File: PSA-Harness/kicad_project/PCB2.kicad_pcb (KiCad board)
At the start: 4 copper layers, 28.3 x 54 mm, 15 parts, among them J1 to_EPS_1, J2 to_EPS_2, J3 to_ESP_3, J7 USB_C_Receptacle, J8 B2B_1, J9 B2B_2, U1 DG419LEUA, U2 DG419LEUA

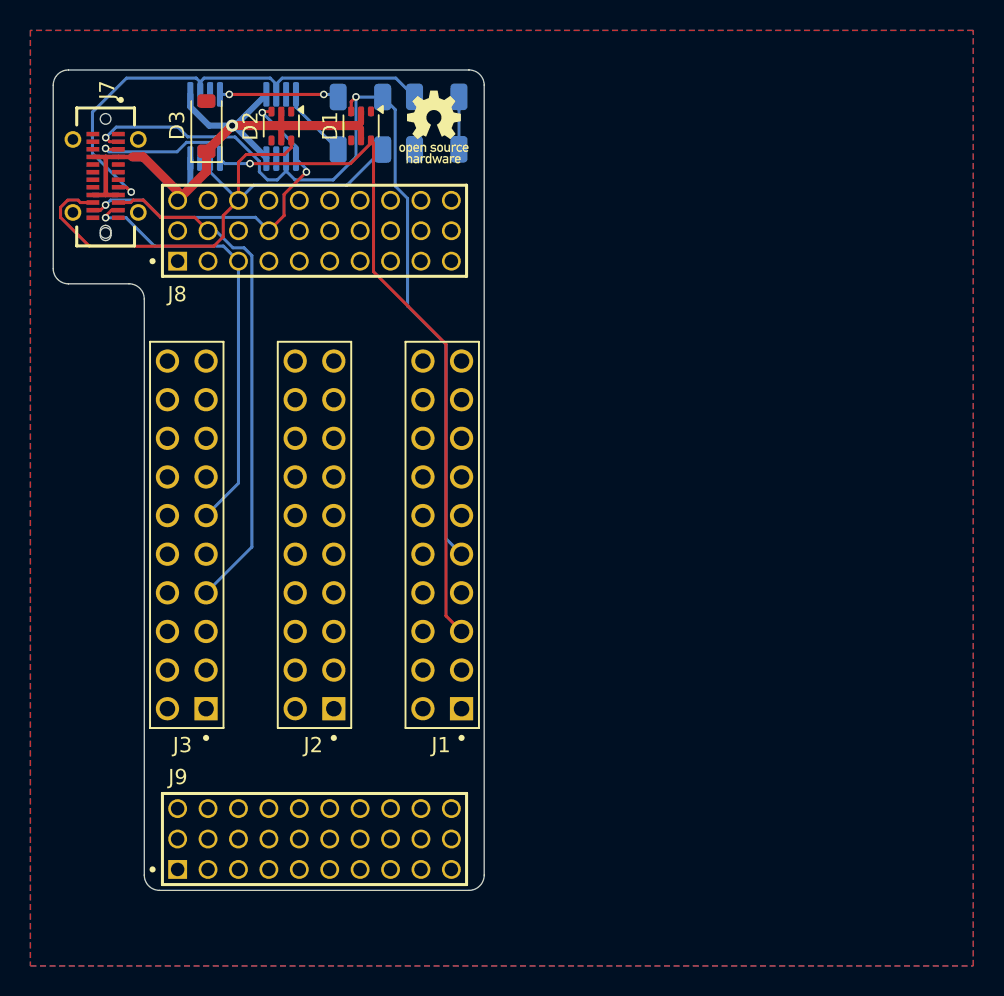
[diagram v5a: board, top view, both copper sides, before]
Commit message: PCB1/2 routed
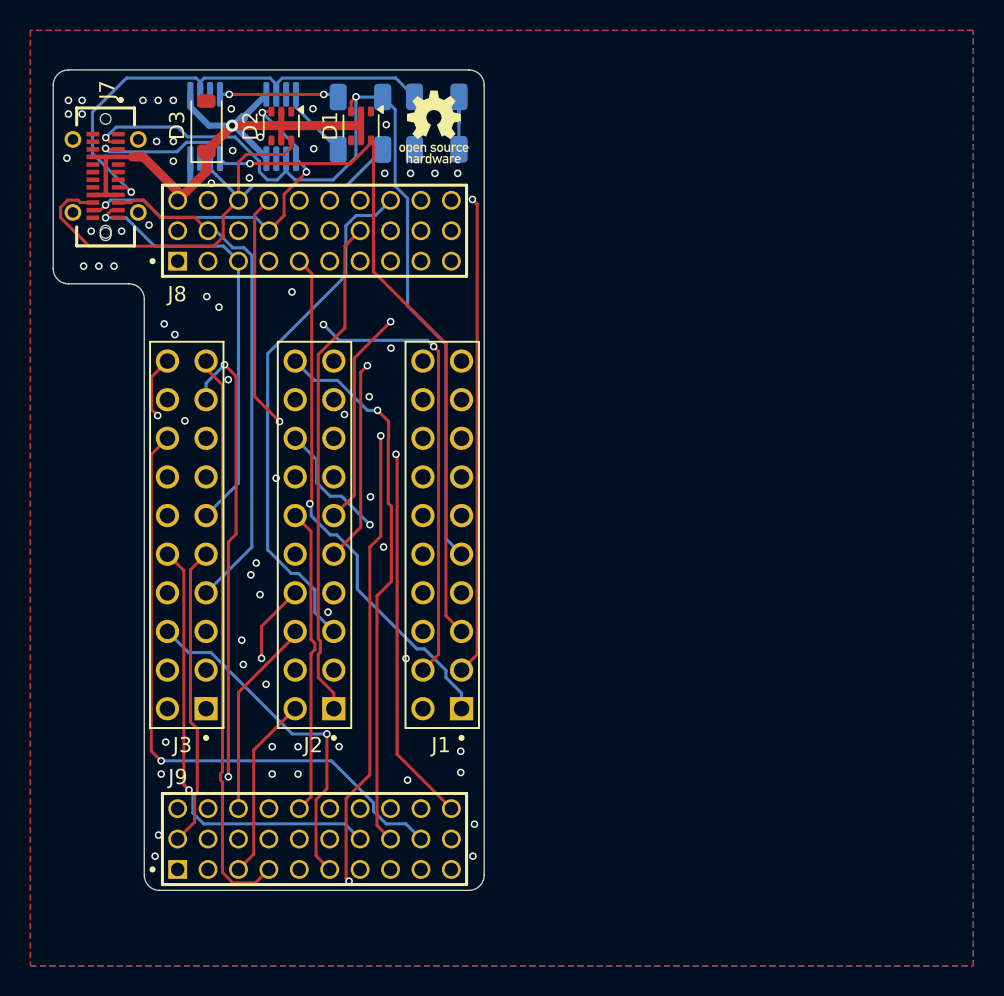
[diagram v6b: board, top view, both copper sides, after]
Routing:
- net 59: track 0.00 -> 47.6 mm, vias 0 -> 1
- net 60: track 0.00 -> 47.4 mm, vias 0 -> 2
- net 28: track 0.00 -> 45.3 mm, vias 0 -> 2
- net 2: track 0.00 -> 43.6 mm, vias 0 -> 1
- net 12: track 0.00 -> 42.1 mm, vias 0 -> 2
- net 58: track 0.00 -> 41.5 mm, vias 0 -> 1
- net 30: track 0.00 -> 38.3 mm, vias 0 -> 1
- net 56: track 0.00 -> 38.0 mm, vias 0 -> 1
- net 50: track 0.00 -> 37.9 mm
- net +12V: track 43.3 -> 81.0 mm
- net 29: track 0.00 -> 36.2 mm, vias 0 -> 1
- net 40: track 0.00 -> 36.1 mm, vias 0 -> 1
- net 14: track 0.00 -> 35.1 mm, vias 0 -> 1
- net 49: track 0.00 -> 35.0 mm, vias 0 -> 2
- net 13: track 0.00 -> 34.7 mm, vias 0 -> 1
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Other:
- rule pad_to_mask_clearance: 0.038 -> 0

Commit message: fix DRC errors
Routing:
- net 33: track 13.2 -> 13.7 mm
- net GND: vias 51 -> 52
